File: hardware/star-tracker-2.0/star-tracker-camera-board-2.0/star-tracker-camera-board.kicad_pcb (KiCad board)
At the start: 4 copper layers, 31.5 x 13.6 mm, 43 parts, among them J1 3-1734742-6, U1 AR0134CSSM00SPCA0, U2 TPS70618DRVR, U3 TPS71928-28DRVT, U4 TPS71928-28DRVT, X1 MC2520Z27.0000C19XSH

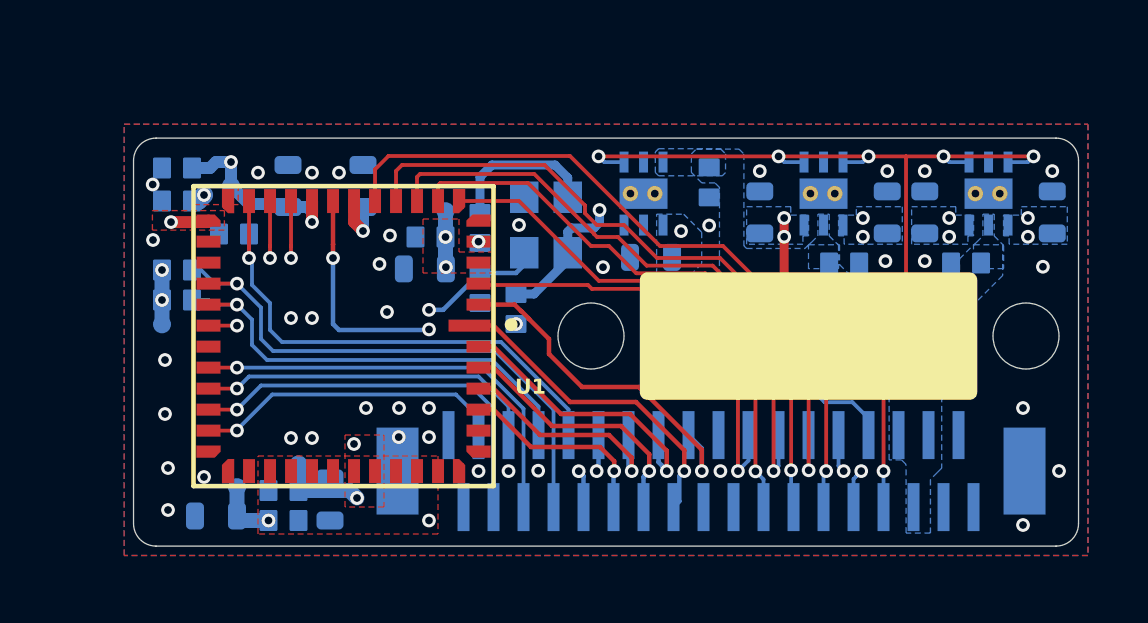
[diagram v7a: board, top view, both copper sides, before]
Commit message: Final Cleanup
Added 3d models to camera and star tracker module. Tightened routing and changed power planes as per DR from Friday.
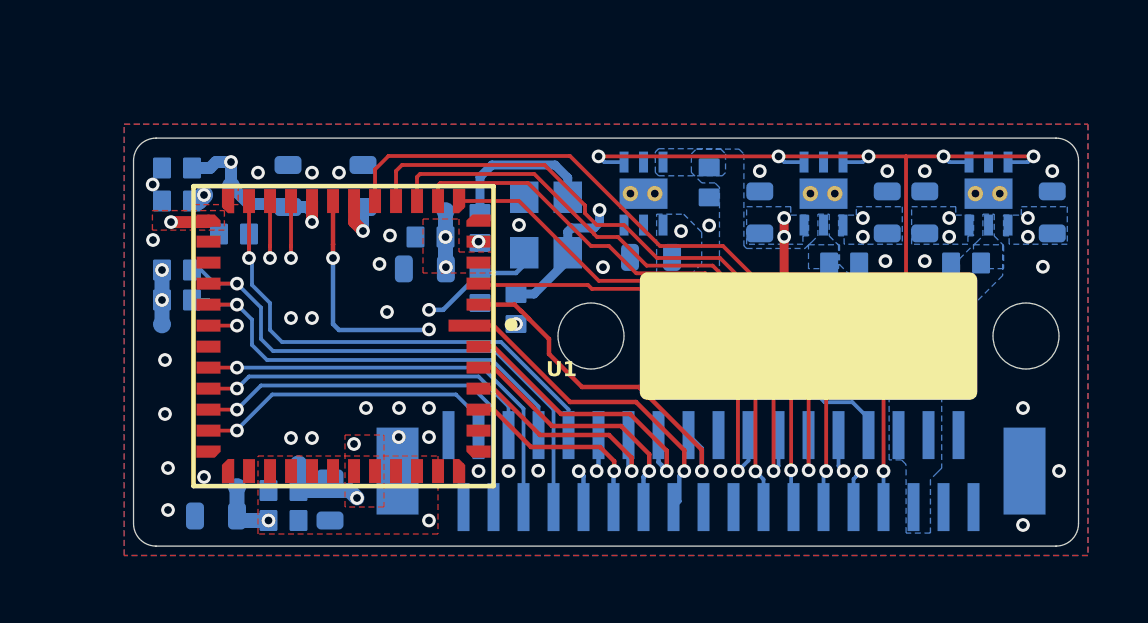
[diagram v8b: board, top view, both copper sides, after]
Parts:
- renumbered C7 to C10, C13 to C11, C11 to C12, C17 to C13, C6 to C14, C10 to C16, C18 to C17, C14 to C18, C4 to C3, C8 to C4, C12 to C5, C16 to C6, C3 to C7, C5 to C8, R10 to R1, R5 to R10, R6 to R11, R9 to R2, R11 to R3, R12 to R4, R8 to R5, R7 to R6, R2 to R7, R3 to R8, R4 to R9, TP6 to TP1, TP7 to TP2, TP8 to TP3, TP9 to TP4, TP10 to TP5
